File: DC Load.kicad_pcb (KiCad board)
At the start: 2 copper layers, 225 x 179.3 mm, 119 parts, among them IC1 REF7050QDGKR, IC10 REF7050QDGKR, IC11 ISO7740FQDBQRQ1, IC12 ISO7741FQDBQRQ1, IC13 INA826AID, IC14 OPA210IDGKR, IC15 INA296A3IDDFR, IC16 MAX31850K, IC17 ISO7741FQDBQRQ1, IC18 ISO7741FQDBQRQ1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

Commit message: added test points
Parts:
- removed C10: 1u, Capacitor_SMD:C_1206_3216Metric
- removed C14: .1u, Capacitor_SMD:C_0603_1608Metric
- removed NT3: NetTie_2, NetTie:NetTie-2_SMD_Pad2.0mm
- added TP1: TestPoint, TestPoint:TestPoint_Pad_SMD-0603, F.Cu at (102.1, 107.0)
- added TP10: TestPoint, TestPoint:TestPoint_Pad_SMD-0603, F.Cu at (221.2, 104.1)
- added TP11: TestPoint, TestPoint:TestPoint_Pad_SMD-0603, F.Cu at (185.7, 103.0)
- added TP12: TestPoint, TestPoint:TestPoint_Keystone_5010-5014_Multipurpose, F.Cu at (58.8, 185.3)
- added TP13: TestPoint, TestPoint:TestPoint_Keystone_5010-5014_Multipurpose, F.Cu at (90.3, 136.6)
- added TP14: TestPoint, TestPoint:TestPoint_Keystone_5010-5014_Multipurpose, F.Cu at (100.4, 167.6)
- added TP15: TestPoint, TestPoint:TestPoint_Keystone_5010-5014_Multipurpose, F.Cu at (201.2, 181.4)
- added TP16: TestPoint, TestPoint:TestPoint_Keystone_5010-5014_Multipurpose, F.Cu at (56.5, 105.5)
- added TP17: TestPoint, TestPoint:TestPoint_Keystone_5010-5014_Multipurpose, F.Cu at (79.4, 43.3)
- added TP18: TestPoint, TestPoint:TestPoint_Keystone_5010-5014_Multipurpose, F.Cu at (219.5, 91.9)
- added TP19: TestPoint, TestPoint:TestPoint_Keystone_5010-5014_Multipurpose, F.Cu at (136.7, 146.3)
- added TP2: TestPoint, TestPoint:TestPoint_Pad_SMD-0603, F.Cu at (82.4, 119.3)
- added TP20: TestPoint, TestPoint:TestPoint_Keystone_5010-5014_Multipurpose, F.Cu at (200.2, 161.3)
- added TP21: TestPoint, TestPoint:TestPoint_Keystone_5010-5014_Multipurpose, F.Cu at (110.6, 73.3)
- added TP22: TestPoint, TestPoint:TestPoint_Keystone_5010-5014_Multipurpose, F.Cu at (102.0, 99.0)
- added TP23: TestPoint, TestPoint:TestPoint_Keystone_5010-5014_Multipurpose, F.Cu at (180.2, 95.3)
- added TP24: TestPoint, TestPoint:TestPoint_Keystone_5010-5014_Multipurpose, F.Cu at (112.7, 41.0)
- added TP25: TestPoint, TestPoint:TestPoint_Keystone_5010-5014_Multipurpose, F.Cu at (121.5, 125.7)
- added TP26: TestPoint, TestPoint:TestPoint_Pad_SMD-0603, F.Cu at (122.6, 138.0)
- added TP27: TestPoint, TestPoint:TestPoint_Pad_SMD-0603, F.Cu at (132.6, 136.3)
- added TP28: TestPoint, TestPoint:TestPoint_Pad_SMD-0603, F.Cu at (128.1, 136.9)
- added TP29: TestPoint, TestPoint:TestPoint_Pad_SMD-0603, F.Cu at (128.3, 143.4)
- added TP3: TestPoint, TestPoint:TestPoint_Pad_SMD-0603, F.Cu at (100.6, 111.9)
- added TP30: TestPoint, TestPoint:TestPoint_Pad_SMD-0603, F.Cu at (222.2, 98.4)
- added TP31: TestPoint, TestPoint:TestPoint_Pad_SMD-0603, F.Cu at (174.7, 128.2)
- added TP32: TestPoint, TestPoint:TestPoint_Pad_SMD-0603, F.Cu at (201.2, 104.0)
- added TP33: TestPoint, TestPoint:TestPoint_Pad_SMD-0603, F.Cu at (202.2, 93.8)
- added TP34: TestPoint, TestPoint:TestPoint_Pad_SMD-0603, F.Cu at (210.0, 92.8)
- added TP35: TestPoint, TestPoint:TestPoint_Pad_SMD-0603, F.Cu at (229.1, 91.9)
- added TP36: TestPoint, TestPoint:TestPoint_Pad_SMD-0603, F.Cu at (235.5, 91.7)
- added TP37: TestPoint, TestPoint:TestPoint_Pad_SMD-0603, F.Cu at (157.3, 78.3)
- added TP38: TestPoint, TestPoint:TestPoint_Pad_SMD-0603, F.Cu at (160.3, 84.0)
- added TP4: TestPoint, TestPoint:TestPoint_Pad_SMD-0603, F.Cu at (88.6, 109.9)
- added TP5: TestPoint, TestPoint:TestPoint_Pad_SMD-0603, F.Cu at (88.5, 122.4)
- added TP6: TestPoint, TestPoint:TestPoint_Pad_SMD-0603, F.Cu at (136.5, 155.1)
- added TP7: TestPoint, TestPoint:TestPoint_Pad_SMD-0603, F.Cu at (135.1, 149.2)
- added TP8: TestPoint, TestPoint:TestPoint_Pad_SMD-0603, F.Cu at (136.9, 158.2)
- added TP9: TestPoint, TestPoint:TestPoint_Pad_SMD-0603, F.Cu at (136.8, 151.5)
- moved C37 24.2 mm to (142.8, 98.8), turned to 90 degrees
- moved C28 22.7 mm to (118.5, 82.3)
- moved C21 22.6 mm to (130.0, 96.1)
- moved C27 22.6 mm to (129.7, 99.8)
- moved IC9 22.6 mm to (136.1, 99.1)
- moved L4 18.7 mm to (104.2, 80.2), turned to -90 degrees
- moved L3 18.7 mm to (116.2, 94.2), turned to 90 degrees
- moved C22 15.1 mm to (111.6, 82.3), turned to 90 degrees
- moved C38 12.6 mm to (136.2, 88.8)
- moved U1 11.7 mm to (126.6, 88.1), turned to 0 degrees
- moved C31 8.15 mm to (160.2, 104.0), turned to 90 degrees
- moved C34 6.46 mm to (155.2, 103.8), turned to 90 degrees
- moved C42 1.71 mm to (155.4, 145.4)
- moved C44 1.71 mm to (160.2, 144.6)
- moved R2 0.35 mm to (201.2, 128.2)
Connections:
- C12 pad 2: DGND Isolated -> GND Isolated
- C42 pad 1: DGND Isolated -> GND Isolated
- C43 pad 2: DGND Isolated -> GND Isolated
- C44 pad 1: DGND Isolated -> GND Isolated
- C45 pad 2: DGND Isolated -> GND Isolated
- C58 pad 2: DGND Isolated -> GND Isolated
- C59 pad 2: DGND Isolated -> GND Isolated
- C67 pad 2: DGND Isolated -> GND Isolated
- C68 pad 2: DGND Isolated -> GND Isolated
- IC11 pad 15: DGND Isolated -> GND Isolated
- IC11 pad 9: DGND Isolated -> GND Isolated
- IC12 pad 15: DGND Isolated -> GND Isolated
- IC12 pad 9: DGND Isolated -> GND Isolated
- IC16 pad 3: DGND Isolated -> GND Isolated
- IC17 pad 15: DGND Isolated -> GND Isolated
- IC17 pad 9: DGND Isolated -> GND Isolated
- IC18 pad 15: DGND Isolated -> GND Isolated
- IC18 pad 9: DGND Isolated -> GND Isolated
- IC2 pad 12: DGND Isolated -> GND Isolated
- IC4 pad 17: DGND Isolated -> GND Isolated
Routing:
- net +3.3V: track 237.7 -> 296.4 mm, vias 9 -> 10
- net +5V Isolated: track 303.9 -> 273.8 mm, vias 8 -> 10
- net +3.3V Isolated: track 260.6 -> 245.0 mm
- net GND Isolated: track 18.4 -> 33.7 mm, vias 61 -> 91
- net +6V Isolated: track 213.5 -> 228.1 mm, vias 6 -> 8
- net DGND Isolated: track 13.0 -> 0.00 mm, vias 26 -> 0
- net Net-(PS3--VOUT): track 18.5 -> 10.8 mm
- net Net-(PS3-+VOUT): track 7.97 -> 14.0 mm
- net Net-(IC9-VIN): track 23.9 -> 28.6 mm
- net +21V Isolated: track 88.7 -> 84.1 mm
- net Sense Amp Ref: track 177.1 -> 180.5 mm
- net Current Sense Amp Out: track 105.9 -> 108.7 mm
- net Voltage Sense -: track 49.3 -> 46.8 mm
- net Sense ~{CS}: track 27.7 -> 30.0 mm
- net Sense CIPO uC: track 36.5 -> 38.5 mm
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- removed copper zone on B.Cu, net DGND Isolated
- removed copper zone on F.Cu, net DGND Isolated
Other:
- outline, holes or cut-outs redrawn

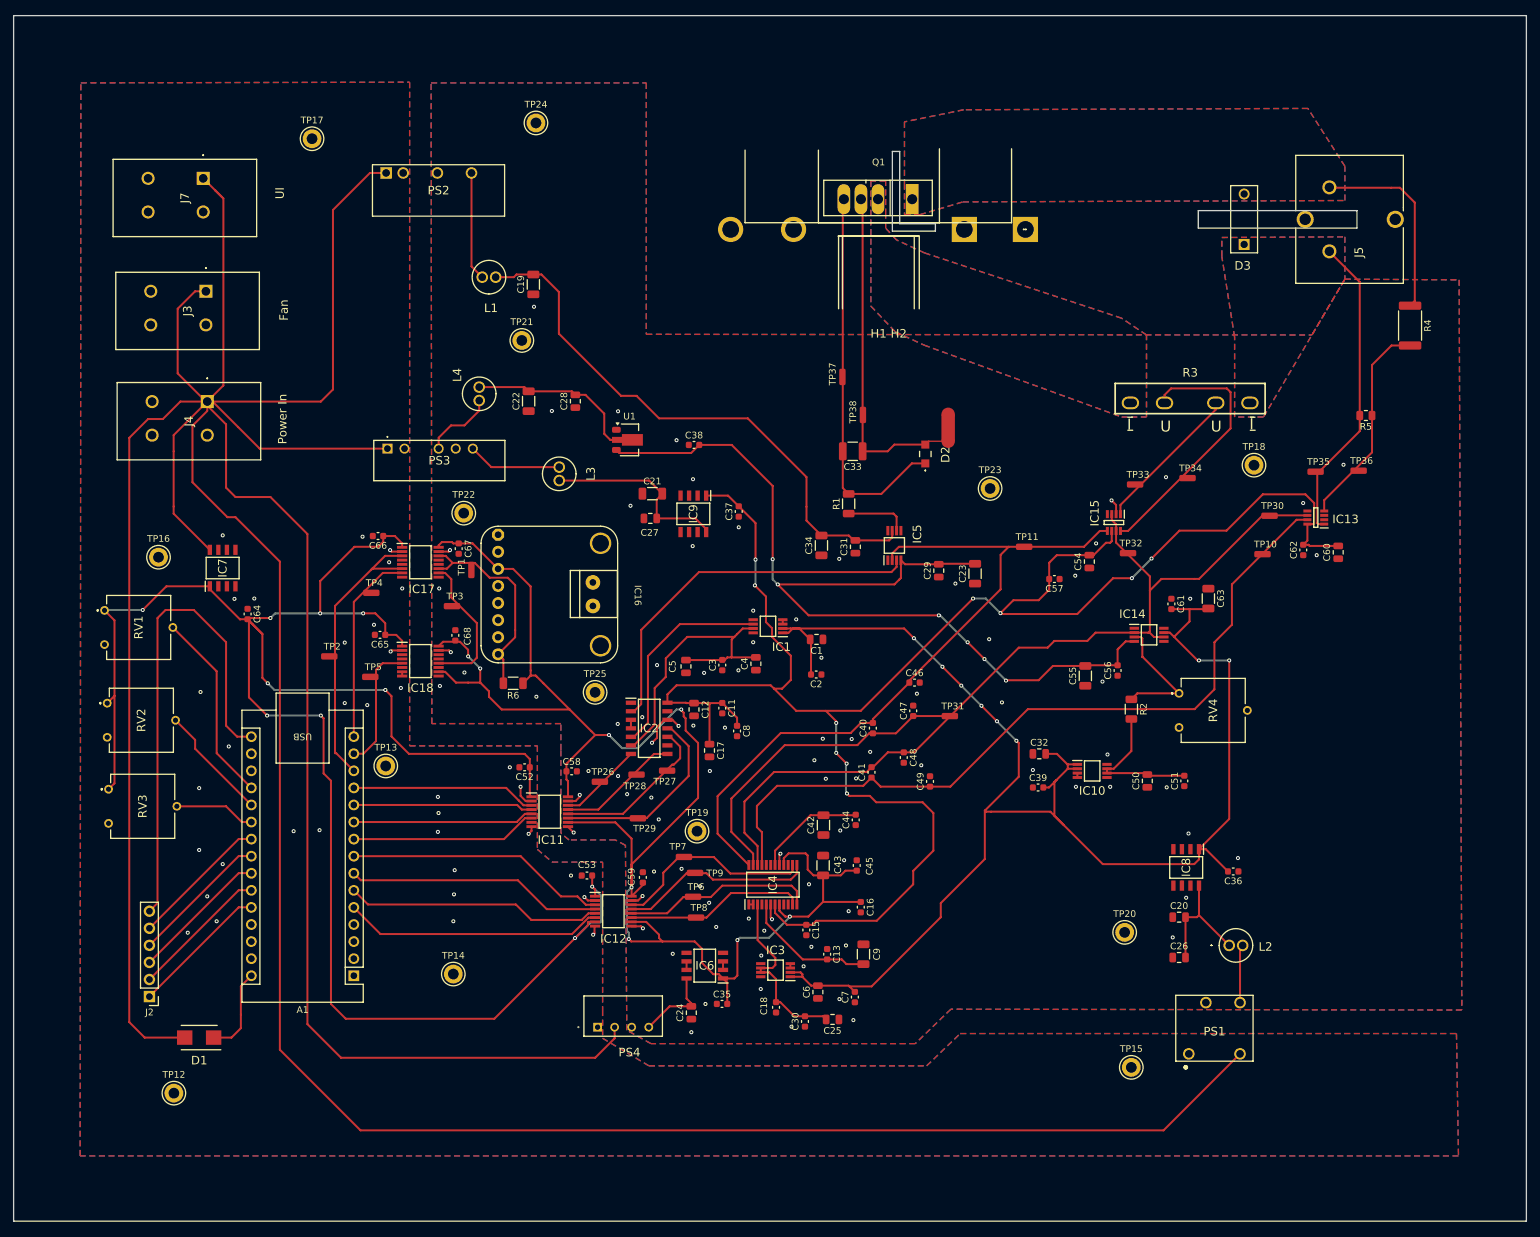
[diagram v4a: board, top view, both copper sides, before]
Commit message: added mounting holes
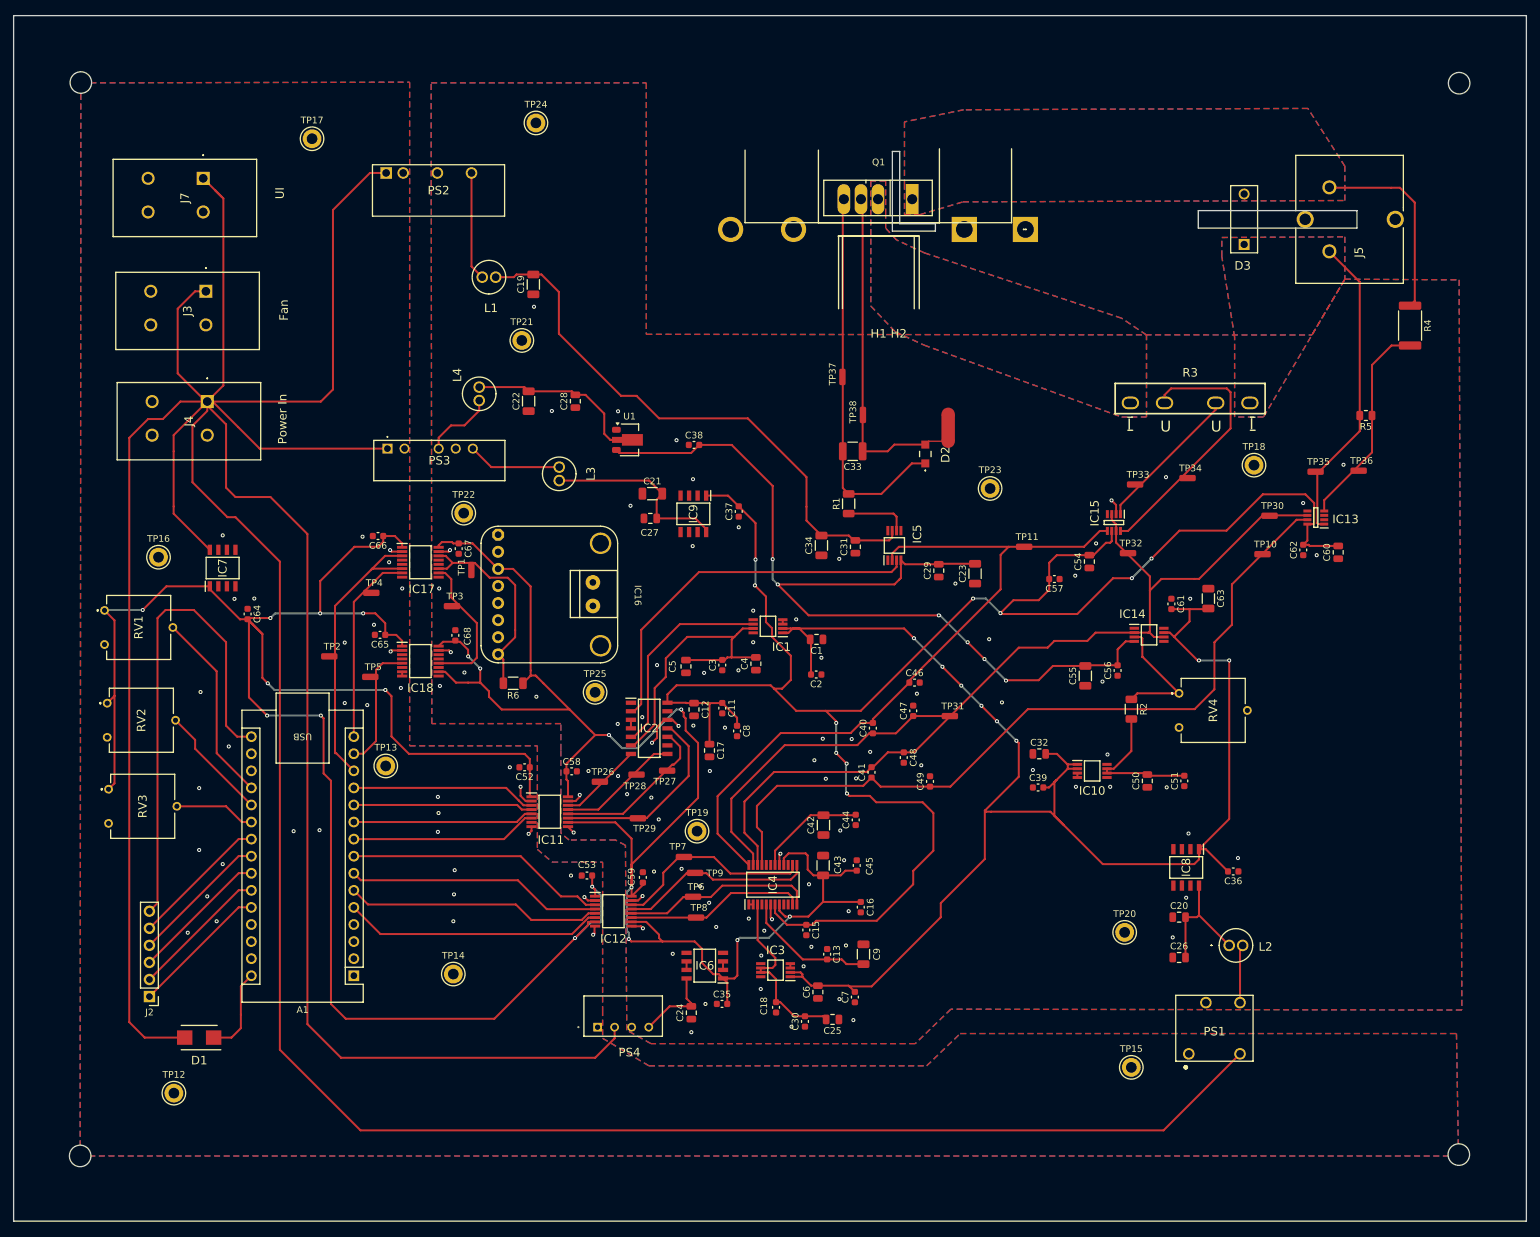
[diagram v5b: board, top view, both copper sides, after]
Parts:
- added REF**: MountingHole_3.2mm_M3, MountingHole:MountingHole_3.2mm_M3, F.Cu at (44.9, 194.6)
- added REF**: MountingHole_3.2mm_M3, MountingHole:MountingHole_3.2mm_M3, F.Cu at (249.9, 194.4)
- added REF**: MountingHole_3.2mm_M3, MountingHole:MountingHole_3.2mm_M3, F.Cu at (250.0, 35.0)
- added REF**: MountingHole_3.2mm_M3, MountingHole:MountingHole_3.2mm_M3, F.Cu at (45.0, 35.0)

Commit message: added 3D models
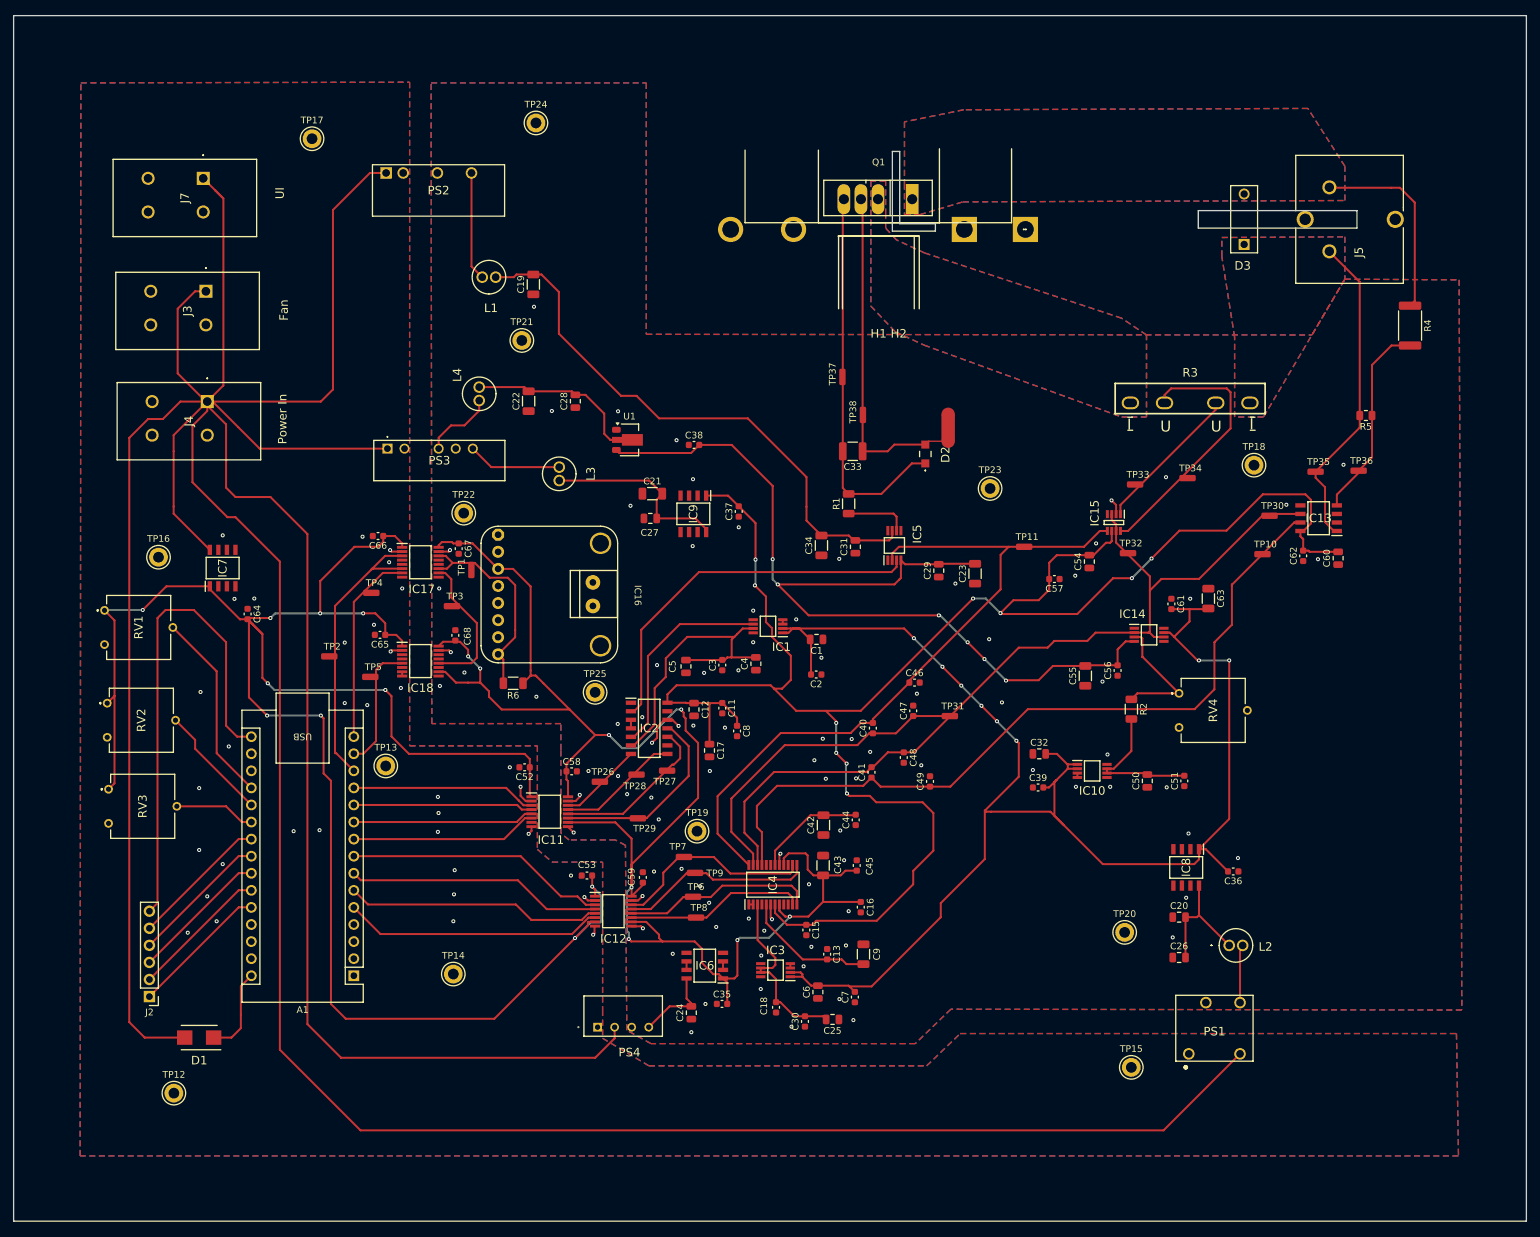
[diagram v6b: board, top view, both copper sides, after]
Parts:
- removed REF** (x4): MountingHole_3.2mm_M3, MountingHole:MountingHole_3.2mm_M3
- IC13: footprint INA296A3IDDFR:SOT65P280X110-8N -> INA826AID:SOIC127P600X175-8N
- moved C60 0.88 mm to (232.0, 105.7)
- moved C62 0.88 mm to (226.8, 105.3)
- moved IC13 0.43 mm to (229.1, 99.8)
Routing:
- net Sense Amp Ref: track 180.5 -> 178.5 mm
- net Voltage Sense -: track 46.8 -> 48.6 mm
- net Voltage Sense +: track 31.5 -> 29.9 mm
- net Voltage Sense Amp Out: track 117.3 -> 116.3 mm
- net +5V Isolated: track 273.8 -> 274.5 mm
